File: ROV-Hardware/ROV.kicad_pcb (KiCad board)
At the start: 2 copper layers, 104 x 104 mm, 17 parts, among them J1 Screw_Terminal_01x02, J2 Screw_Terminal_01x02, J3 Screw_Terminal_01x04, SW1 SW_Wuerth_450301014042, U1 LM7812_TO220, U2 LM7805_TO220, U3 ESP32-S3-DEVKITC-1-N8R2, U4 MPU6050, U5 ZK-BM!, U6 ZK-BM!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

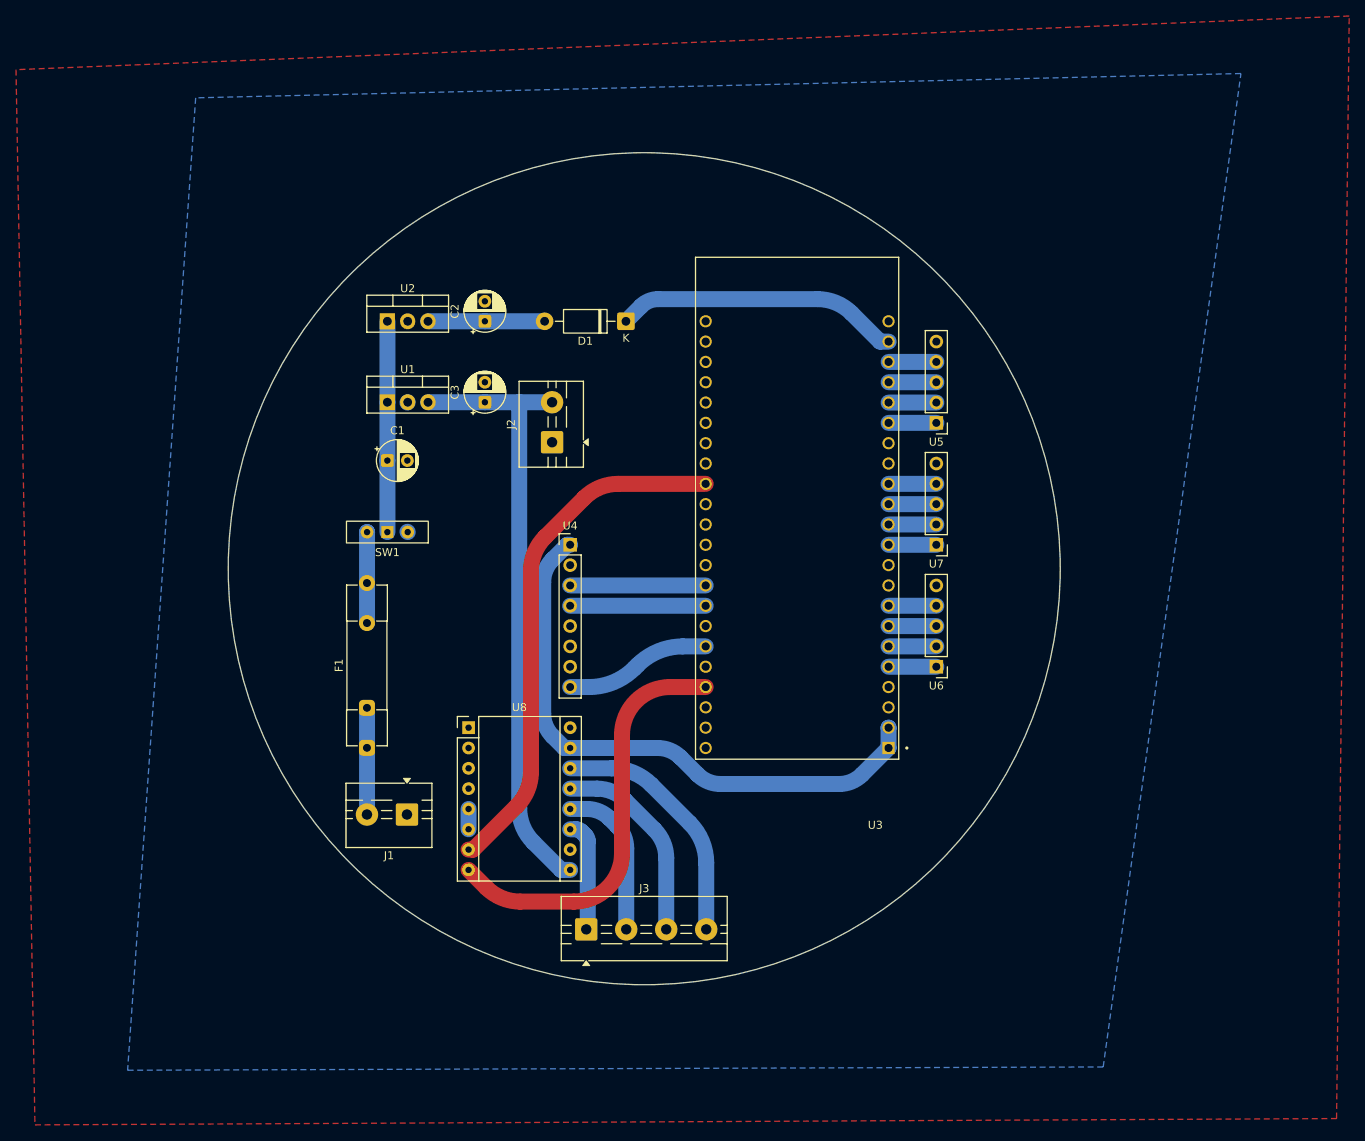
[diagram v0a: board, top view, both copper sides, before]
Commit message: Here I added GM-MS5837
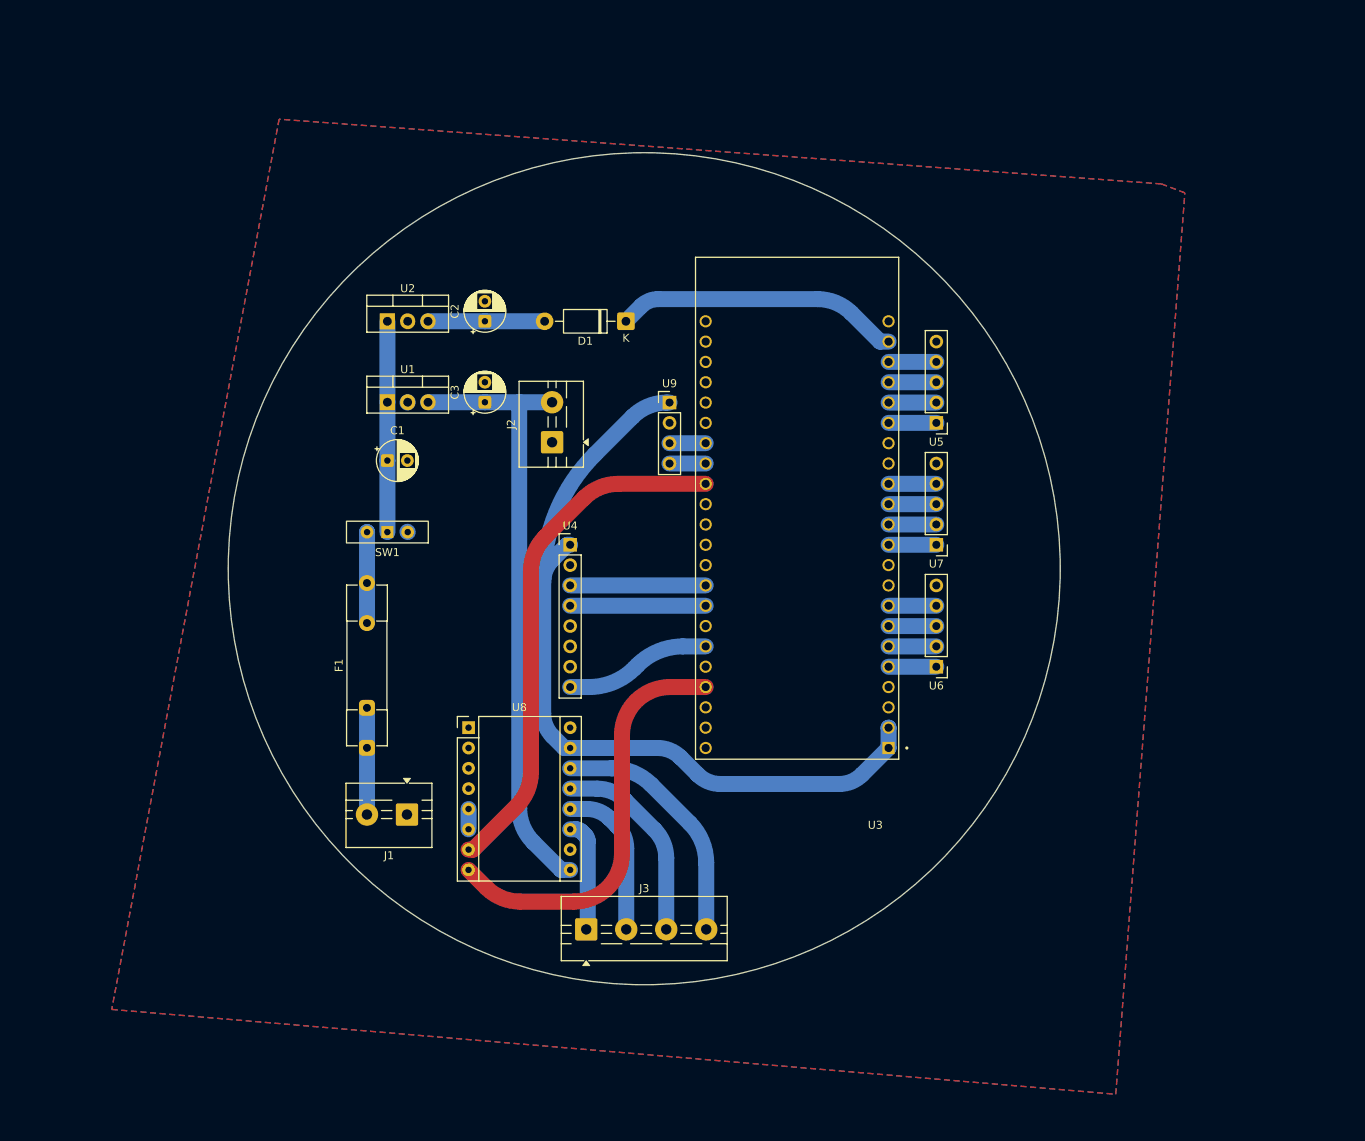
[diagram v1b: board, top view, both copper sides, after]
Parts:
- added U9: ~, Connector_PinHeader_2.54mm:PinHeader_1x04_P2.54mm_Vertical, F.Cu at (117.4, 100.6)
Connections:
- U3 pad J3_15: unconnected-(U3-GPIO45-PadJ3_15) -> Net-(U3-GPIO45)
- U3 pad J3_16: unconnected-(U3-GPIO48-PadJ3_16) -> Net-(U3-GPIO48)
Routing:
- net +3.3V: track 73.9 -> 103.2 mm
- net Net-(U3-GPIO48): track 0.00 -> 4.52 mm
- net Net-(U3-GPIO45): track 0.00 -> 4.52 mm

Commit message: refresh
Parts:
- added D2: LED, LED_THT:LED_D3.0mm, F.Cu at (76.0, 107.8)
- added D3: LED, LED_THT:LED_D3.0mm, F.Cu at (102.7, 90.4)
- added D4: LED, LED_THT:LED_D3.0mm, F.Cu at (102.7, 100.5)
- added D5: LED, LED_THT:LED_D3.0mm, F.Cu at (72.3, 116.8)
- added F2: fuse, Fuse:Fuseholder_Clip-5x20mm_Schurter_CQM_Inline_P20.60x5.00mm_D1.00mm_Horizontal, F.Cu at (87.2, 81.6)
- added G***: LOGO, logo:englogo4, F.Cu at (133.9, 159.2)
- added G***: LOGO, logo:logo7, F.Cu at (158.1, 121.3)
- added G***: LOGO, logo:logo7, B.Cu at (133.3, 114.9)
- added G***: LOGO, logo:englogo3, B.Cu at (133.5, 134.6)
- added R1: R, Resistor_THT:R_Axial_DIN0204_L3.6mm_D1.6mm_P5.08mm_Horizontal, F.Cu at (67.9, 107.8)
- added R2: R, Resistor_THT:R_Axial_DIN0204_L3.6mm_D1.6mm_P5.08mm_Horizontal, F.Cu at (110.8, 90.4)
- added R3: R, Resistor_THT:R_Axial_DIN0204_L3.6mm_D1.6mm_P5.08mm_Horizontal, F.Cu at (110.8, 100.5)
- added R4: R, Resistor_THT:R_Axial_DIN0204_L3.6mm_D1.6mm_P5.08mm_Horizontal, F.Cu at (69.4, 121.8)
- C1, C2, C3: value C_Polarized -> capacitor
- F1: value Fuse -> fuse
- J1: value Screw_Terminal_01x02 -> T-block; footprint TerminalBlock:TerminalBlock_MaiXu_MX126-5.0-02P_1x02_P5.00mm -> Connector_AMASS:AMASS_XT60-F_1x02_P7.20mm_Vertical
- J2: value Screw_Terminal_01x02 -> T-block
- SW1: value SW_Wuerth_450301014042 -> switch
- U1: value LM7812_TO220 -> LM7812
- U2: value LM7805_TO220 -> LM7805
- U5, U6, U7: value ZK-BM! -> ZK-BM1
- U8: value ~ -> A4988
- U9: value ~ -> GY-MS5837
- moved F1 22.8 mm to (92.5, 124.9), turned to 180 degrees
- moved D1 17.3 mm to (119.3, 74.7)
- moved J2 11.1 mm to (94.3, 112.8)
- moved J1 8.13 mm to (82.2, 144.3), turned to 90 degrees
- turned C2 to -90 degrees
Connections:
- net /Power1 renamed Net-(D5-A)
- net /Power2 renamed Net-(D2-A)
- net /Power4 renamed Net-(D4-A)
- C2 pad 1: /Power3 -> Net-(D3-A)
- D1 pad 2: /Power3 -> Net-(D1-A)
- U2 pad 3: /Power3 -> Net-(D3-A)
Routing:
- net Net-(D3-A): track 0.00 -> 186.7 mm
- net Net-(D4-A): track 77.0 -> 236.3 mm
- net +12V: track 13.3 -> 104.7 mm
- net Net-(D2-A): track 26.3 -> 89.2 mm
- net Net-(D1-A): track 0.00 -> 59.3 mm
- net Net-(D5-A): track 11.4 -> 48.9 mm
- net +5V: track 35.7 -> 65.0 mm
- net Net-(U3-MTMS/GPIO42): track 18.3 -> 36.5 mm
- net Net-(U3-MTDO/GPIO40): track 16.9 -> 33.9 mm
- net Net-(U3-MTCK/GPIO39): track 16.9 -> 33.9 mm
- net /Power3: track 14.6 -> 0.00 mm
- net +3.3V: track 103.2 -> 113.2 mm
- net Net-(D4-K): track 0.00 -> 6.12 mm
- net Net-(D3-K): track 0.00 -> 6.12 mm
- net Net-(D2-K): track 0.00 -> 6.12 mm
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
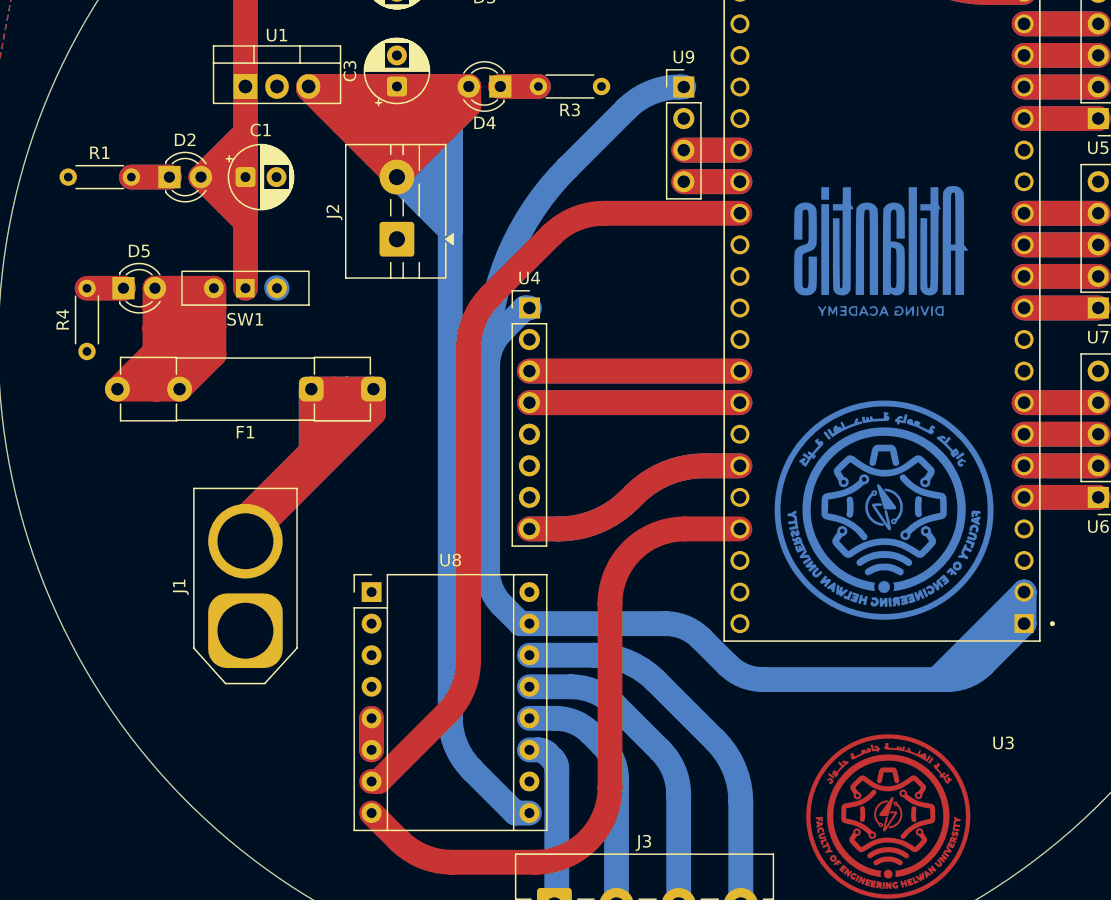
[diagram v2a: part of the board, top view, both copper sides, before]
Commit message: moving controle file to ESP folder
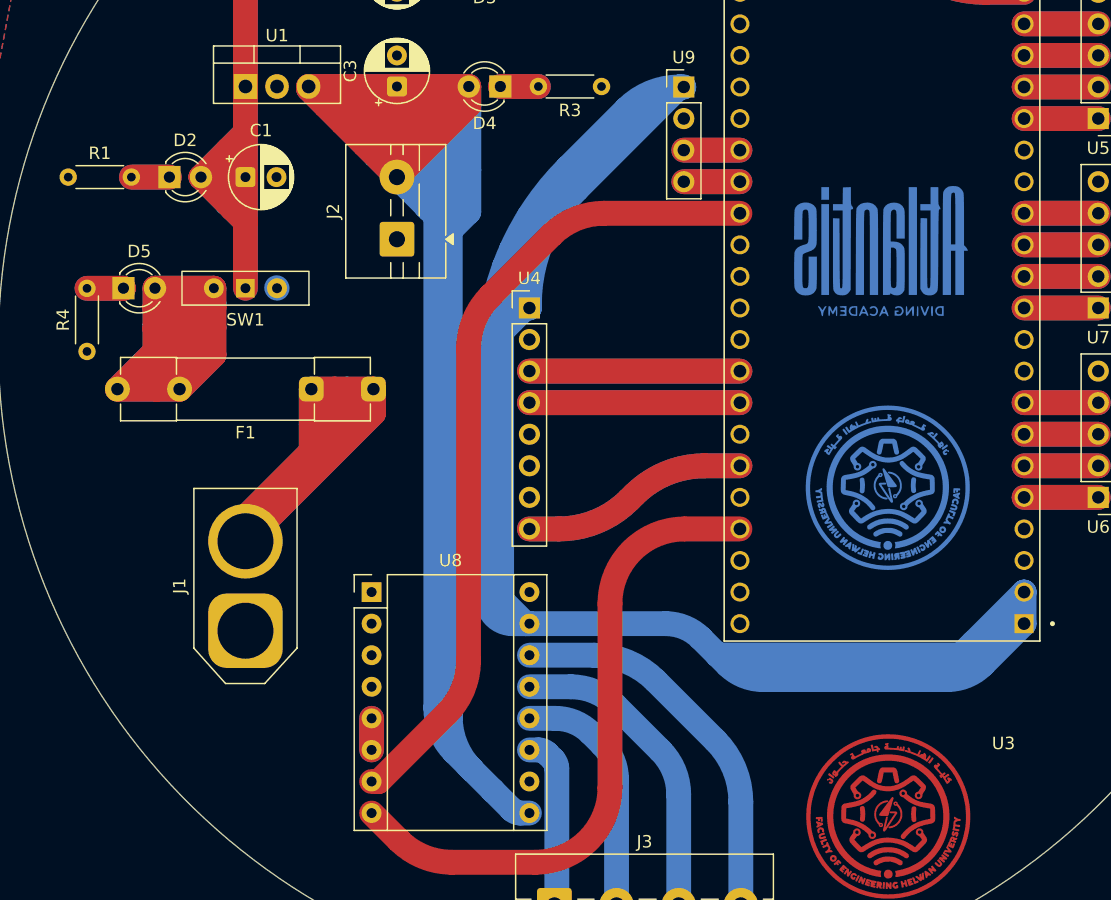
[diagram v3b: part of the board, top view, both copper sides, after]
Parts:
- removed the G*** at (133.5, 134.6)
- added G***: LOGO, logo:englogo4, B.Cu at (133.8, 132.8)
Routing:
- net +3.3V: track 113.2 -> 203.6 mm
- net Net-(D4-A): track 236.3 -> 297.3 mm
- net Net-(D5-A): track 48.9 -> 100.5 mm
- net Net-(D5-K): track 2.93 -> 5.87 mm
